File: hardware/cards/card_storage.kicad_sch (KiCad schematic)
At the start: 21 parts, among them J1 Conn_02x20_Odd_Even, J2 Conn_02x25_Odd_Even, U1 74HCT04, U10 74HCT573, U2 74HCT08, U3 74HCT08, U4 74HCT32, U5 74HCT125, U6 74HCT138, U7 74HCT138, U8 74HCT245, U9 74HCT573

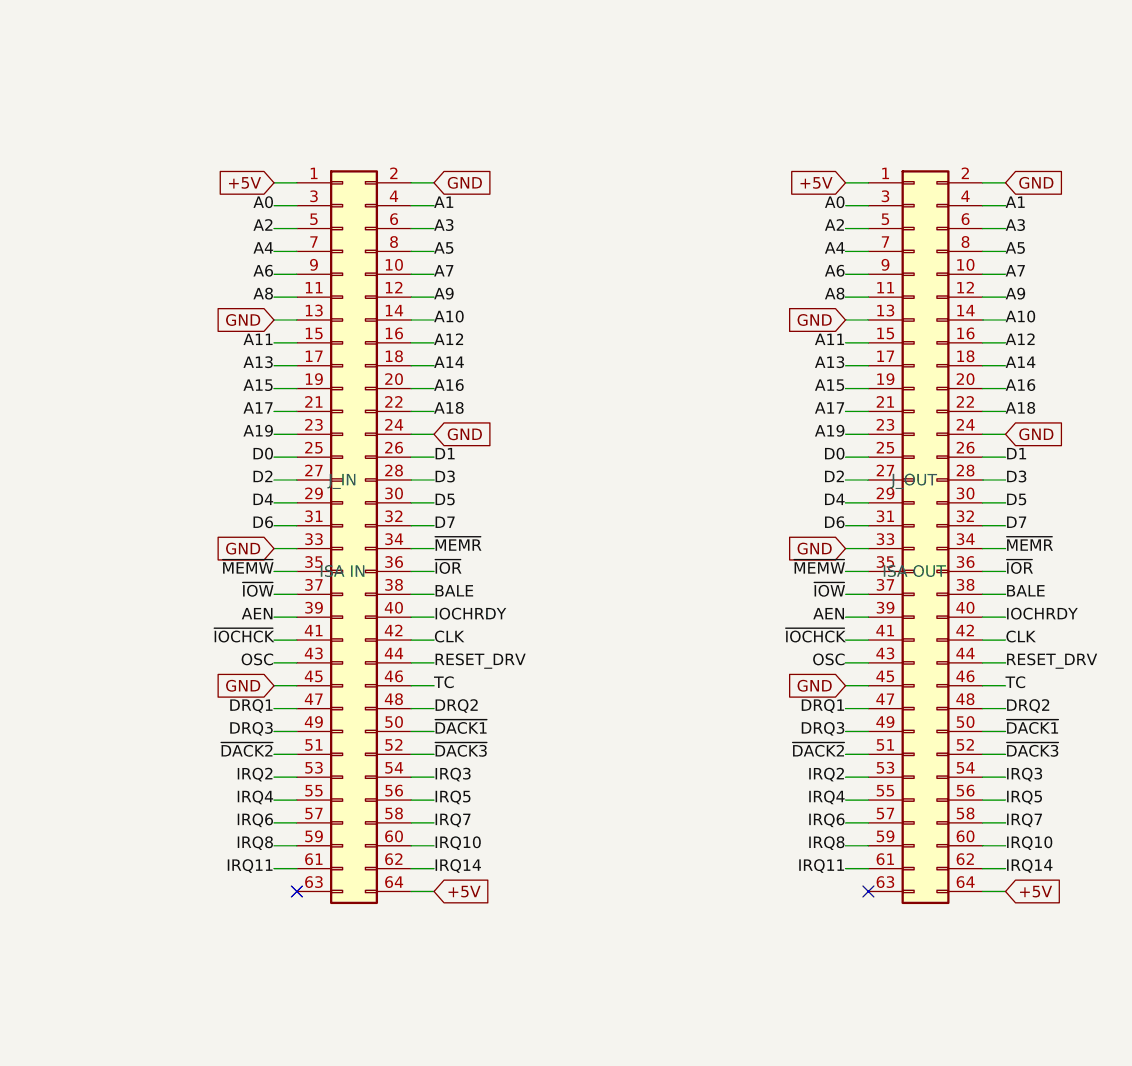
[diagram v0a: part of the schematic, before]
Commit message: Re-base ISA connector on standard 8-bit ISA pinout (60-pin, PicoGUS-style)
isa_conn now uses the standard 8-bit ISA edge pinout on a 60-pin 2.54mm header
(Conn_02x30_Odd_Even), matching the PicoGUS Bus_ISA_8bit layout so the sidecar and
dev cards are pin-compatible with real ISA cards (and 60-pin ribbon is easy to
source). The unused ISA analog rails are reclaimed: pin7 -5V->~{IOCHCK}, pin11
-12V->GND (extra return), pin15 +12V->IRQ8; pin13 reserved/0WS# left NC. Drops the
non-standard IRQ10/11/14 (16-bit-extension signals on a real AT); DACK0/REFRESH#
now on its standard pin (undriven, for card compatibility). Change is confined to
isa_conn.py; sidecar + all card_* sheets inherit it. Verified pin map and
connectivity (IOCHCK->Bus MCU, IRQ8->collector+RTC); zero structural ERC on
motherboard and all five cards.

Co-Authored-By: Claude Opus 4.8 (1M context) <noreply@anthropic.com>
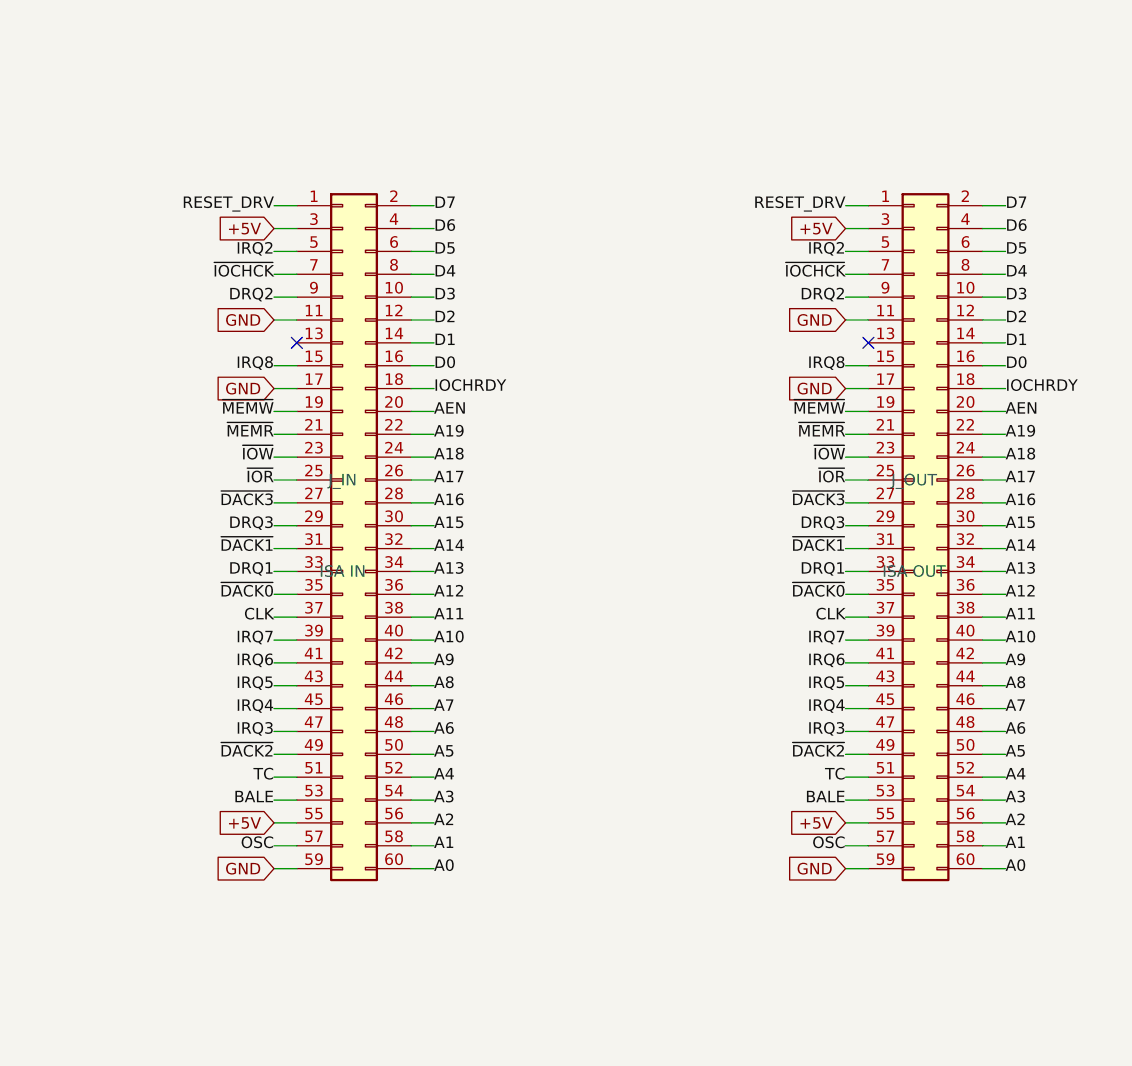
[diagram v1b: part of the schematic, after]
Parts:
- removed J_IN: ISA IN, symbol Connector_Generic:Conn_02x32_Odd_Even
- removed J_OUT: ISA OUT, symbol Connector_Generic:Conn_02x32_Odd_Even
- added J_IN: ISA IN, symbol Connector_Generic:Conn_02x30_Odd_Even
- added J_OUT: ISA OUT, symbol Connector_Generic:Conn_02x30_Odd_Even
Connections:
- net +5V: now also J_IN.3 (Pin_3), J_IN.55 (Pin_55), J_OUT.3 (Pin_3), J_OUT.55 (Pin_55)
- net A0: now also J_IN.60 (Pin_60), J_OUT.60 (Pin_60)
- net A1: now also J_IN.58 (Pin_58), J_OUT.58 (Pin_58)
- net A10: now also J_IN.40 (Pin_40), J_OUT.40 (Pin_40)
- net A11: now also J_IN.38 (Pin_38), J_OUT.38 (Pin_38)
- net A12: now also J_IN.36 (Pin_36), J_OUT.36 (Pin_36)
- net A13: now also J_IN.34 (Pin_34), J_OUT.34 (Pin_34)
- net A14: now also J_IN.32 (Pin_32), J_OUT.32 (Pin_32)
- net A15: now also J_IN.30 (Pin_30), J_OUT.30 (Pin_30)
- net A16: now also J_IN.28 (Pin_28), J_OUT.28 (Pin_28)
- net A17: now also J_IN.26 (Pin_26), J_OUT.26 (Pin_26)
- net A18: now also J_IN.24 (Pin_24), J_OUT.24 (Pin_24)
- net A19: now also J_IN.22 (Pin_22), J_OUT.22 (Pin_22)
- net A2: now also J_IN.56 (Pin_56), J_OUT.56 (Pin_56)
- net A3: now also J_IN.54 (Pin_54), J_OUT.54 (Pin_54)
- net A4: now also J_IN.52 (Pin_52), J_OUT.52 (Pin_52)
- net A5: now also J_IN.50 (Pin_50), J_OUT.50 (Pin_50)
- net A6: now also J_IN.48 (Pin_48), J_OUT.48 (Pin_48)
- net A7: now also J_IN.46 (Pin_46), J_OUT.46 (Pin_46)
- net A8: now also J_IN.44 (Pin_44), J_OUT.44 (Pin_44)
- net A9: now also J_IN.42 (Pin_42), J_OUT.42 (Pin_42)
- net AEN: now also J_IN.20 (Pin_20), J_OUT.20 (Pin_20)
- net BALE: now also J_IN.53 (Pin_53), J_OUT.53 (Pin_53)
- net CLK: now also J_IN.37 (Pin_37), J_OUT.37 (Pin_37)
- net D0: now also J_IN.16 (Pin_16), J_OUT.16 (Pin_16)
- net D1: now also J_IN.14 (Pin_14), J_OUT.14 (Pin_14)
- net D2: now also J_IN.12 (Pin_12), J_OUT.12 (Pin_12)
- net D3: now also J_IN.10 (Pin_10), J_OUT.10 (Pin_10)
- net D4: now also J_IN.8 (Pin_8), J_OUT.8 (Pin_8)
- net D5: now also J_IN.6 (Pin_6), J_OUT.6 (Pin_6)
- net D6: now also J_IN.4 (Pin_4), J_OUT.4 (Pin_4)
- net D7: now also J_IN.2 (Pin_2), J_OUT.2 (Pin_2)
- net DRQ1: now also J_IN.33 (Pin_33), J_OUT.33 (Pin_33)
- net DRQ2: now also J_IN.9 (Pin_9), J_OUT.9 (Pin_9)
- net DRQ3: now also J_IN.29 (Pin_29), J_OUT.29 (Pin_29)
- net GND: now also J_IN.11 (Pin_11), J_IN.17 (Pin_17), J_IN.59 (Pin_59), J_OUT.11 (Pin_11), J_OUT.17 (Pin_17), J_OUT.59 (Pin_59)
- net IOCHRDY: now also J_IN.18 (Pin_18), J_OUT.18 (Pin_18)
- net IRQ2: now also J_IN.5 (Pin_5), J_OUT.5 (Pin_5)
- net IRQ3: now also J_IN.47 (Pin_47), J_OUT.47 (Pin_47)
- net IRQ4: now also J_IN.45 (Pin_45), J_OUT.45 (Pin_45)
- net IRQ5: now also J_IN.43 (Pin_43), J_OUT.43 (Pin_43)
- net IRQ6: now also J_IN.41 (Pin_41), J_OUT.41 (Pin_41)
- net IRQ7: now also J_IN.39 (Pin_39), J_OUT.39 (Pin_39)
- net IRQ8: now also J_IN.15 (Pin_15), J_OUT.15 (Pin_15)
- net OSC: now also J_IN.57 (Pin_57), J_OUT.57 (Pin_57)
- net RESET_DRV: now also J_IN.1 (Pin_1), J_OUT.1 (Pin_1)
- net TC: now also J_IN.51 (Pin_51), J_OUT.51 (Pin_51)
- net ~{DACK1}: now also J_IN.31 (Pin_31), J_OUT.31 (Pin_31)
- net ~{DACK2}: now also J_IN.49 (Pin_49), J_OUT.49 (Pin_49)
- net ~{DACK3}: now also J_IN.27 (Pin_27), J_OUT.27 (Pin_27)
- net ~{IOCHCK}: now also J_IN.7 (Pin_7), J_OUT.7 (Pin_7)
- net ~{IOR}: now also J_IN.25 (Pin_25), J_OUT.25 (Pin_25)
- net ~{IOW}: now also J_IN.23 (Pin_23), J_OUT.23 (Pin_23)
- net ~{MEMR}: now also J_IN.21 (Pin_21), J_OUT.21 (Pin_21)
- net ~{MEMW}: now also J_IN.19 (Pin_19), J_OUT.19 (Pin_19)
- new net ~{DACK0}: J_IN.35 (Pin_35), J_OUT.35 (Pin_35)

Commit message: Drive ISA REFRESH# from the Bus MCU for DRAM-based cards
Pin 35 (DACK0/REFRESH#) net renamed ~{DACK0} -> ~{REFRESH} in isa_conn and is now
an active Bus MCU output (GPIO47, reclaimed from the redundant raw-~WR sense -- the
MCU tracks writes via the gated MEMW/IOW). Driven from the internal ~15us refresh
timer (same source as the 0x61-bit-4 toggle); a refresh cycle reuses the bus-master
engine to walk the row address on A0-A7 + pulse MEMR#, so DRAM ISA cards see a
standard refresh. ~{REFRESH} added to the Bus MCU interface. Verified it ties
sidecar<->Bus MCU and passes through J_IN<->J_OUT on every dev card; zero
structural ERC on motherboard and all five cards.

Co-Authored-By: Claude Opus 4.8 (1M context) <noreply@anthropic.com>
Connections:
- net ~{DACK0} renamed ~{REFRESH}
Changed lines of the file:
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@@
 		)
 	)
-	(label "~{DACK0}"
+	(label "~{REFRESH}"
 		(at 436.88 160.02 180)
 		(effects
@@
 		)
 	)
-	(label "~{DACK0}"
+	(label "~{REFRESH}"
 		(at 500.38 160.02 180)
 		(effects
@@
 		(instances
 			(project "card_storage"
-				(path "/ed5bbf70-1969-4673-8544-46a05cfa253c"
+				(path "/8a872234-6dda-4e68-94cb-1b220b28d7f7"
 					(reference "J_IN")
 					(unit 1)
@@
 		(instances
 			(project "card_storage"
-				(path "/ed5bbf70-1969-4673-8544-46a05cfa253c"
+				(path "/8a872234-6dda-4e68-94cb-1b220b28d7f7"
 					(reference "J_OUT")
 					(unit 1)
@@
 		(instances
 			(project "card_storage"
-				(path "/ed5bbf70-1969-4673-8544-46a05cfa253c"
+				(path "/8a872234-6dda-4e68-94cb-1b220b28d7f7"
 					(reference "U1")
 					(unit 1)
@@
 		(instances
 			(project "card_storage"
-				(path "/ed5bbf70-1969-4673-8544-46a05cfa253c"
+				(path "/8a872234-6dda-4e68-94cb-1b220b28d7f7"
 					(reference "U2")
 					(unit 1)
@@
 		(instances
 			(project "card_storage"
-				(path "/ed5bbf70-1969-4673-8544-46a05cfa253c"
+				(path "/8a872234-6dda-4e68-94cb-1b220b28d7f7"
 					(reference "U3")
 					(unit 1)
@@
 		(instances
 			(project "card_storage"
-				(path "/ed5bbf70-1969-4673-8544-46a05cfa253c"
+				(path "/8a872234-6dda-4e68-94cb-1b220b28d7f7"
 					(reference "U4")
 					(unit 1)
@@
 		(instances
 			(project "card_storage"
-				(path "/ed5bbf70-1969-4673-8544-46a05cfa253c"
+				(path "/8a872234-6dda-4e68-94cb-1b220b28d7f7"
 					(reference "U5")
 					(unit 1)
@@
 		(instances
 			(project "card_storage"
-				(path "/ed5bbf70-1969-4673-8544-46a05cfa253c"
+				(path "/8a872234-6dda-4e68-94cb-1b220b28d7f7"
 					(reference "U6")
 					(unit 1)
@@
 		(instances
 			(project "card_storage"
-				(path "/ed5bbf70-1969-4673-8544-46a05cfa253c"
+				(path "/8a872234-6dda-4e68-94cb-1b220b28d7f7"
 					(reference "U7")
 					(unit 1)
@@
 		(instances
 			(project "card_storage"
-				(path "/ed5bbf70-1969-4673-8544-46a05cfa253c"
+				(path "/8a872234-6dda-4e68-94cb-1b220b28d7f7"
 					(reference "U8")
 					(unit 1)
@@
 		(instances
 			(project "card_storage"
-				(path "/ed5bbf70-1969-4673-8544-46a05cfa253c"
+				(path "/8a872234-6dda-4e68-94cb-1b220b28d7f7"
 					(reference "U9")
 					(unit 1)
@@
 		(instances
 			(project "card_storage"
-				(path "/ed5bbf70-1969-4673-8544-46a05cfa253c"
+				(path "/8a872234-6dda-4e68-94cb-1b220b28d7f7"
 					(reference "U10")
 					(unit 1)
@@
 		(instances
 			(project "card_storage"
-				(path "/ed5bbf70-1969-4673-8544-46a05cfa253c"
+				(path "/8a872234-6dda-4e68-94cb-1b220b28d7f7"
 					(reference "J1")
 					(unit 1)
@@
 		(instances
 			(project "card_storage"
-				(path "/ed5bbf70-1969-4673-8544-46a05cfa253c"
+				(path "/8a872234-6dda-4e68-94cb-1b220b28d7f7"
 					(reference "J2")
 					(unit 1)
@@
 		(instances
 			(project "card_storage"
-				(path "/ed5bbf70-1969-4673-8544-46a05cfa253c"
+				(path "/8a872234-6dda-4e68-94cb-1b220b28d7f7"
 					(reference "R1")
 					(unit 1)
@@
 		(instances
 			(project "card_storage"
-				(path "/ed5bbf70-1969-4673-8544-46a05cfa253c"
+				(path "/8a872234-6dda-4e68-94cb-1b220b28d7f7"
 					(reference "R2")
 					(unit 1)
@@
 		(instances
 			(project "card_storage"
-				(path "/ed5bbf70-1969-4673-8544-46a05cfa253c"
+				(path "/8a872234-6dda-4e68-94cb-1b220b28d7f7"
 					(reference "R3")
 					(unit 1)
@@
 		(instances
 			(project "card_storage"
-				(path "/ed5bbf70-1969-4673-8544-46a05cfa253c"
+				(path "/8a872234-6dda-4e68-94cb-1b220b28d7f7"
 					(reference "C1")
 					(unit 1)
@@
 		(instances
 			(project "card_storage"
-				(path "/ed5bbf70-1969-4673-8544-46a05cfa253c"
+				(path "/8a872234-6dda-4e68-94cb-1b220b28d7f7"
 					(reference "C2")
 					(unit 1)
@@
 		(instances
 			(project "card_storage"
-				(path "/ed5bbf70-1969-4673-8544-46a05cfa253c"
+				(path "/8a872234-6dda-4e68-94cb-1b220b28d7f7"
 					(reference "C3")
 					(unit 1)
@@
 		(instances
 			(project "card_storage"
-				(path "/ed5bbf70-1969-4673-8544-46a05cfa253c"
+				(path "/8a872234-6dda-4e68-94cb-1b220b28d7f7"
 					(reference "C4")
 					(unit 1)

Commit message: Fix all critical+high design-review findings (C1-C5, H1-H8)
Full review in hardware/notes/design-review-2026-07-03.md (with per-item
fix logs). Highlights:
- SRAM strobed by gated MEMR/MEMW (was raw ~RD/~WR: I/O cycles corrupted
  SRAM and the boot shadow-load could never write it)
- Reset chain implemented: NAND combine of ~PWRGOOD + ~CPURESET drives
  V20 RESET and an always-driven RESET_DRV (dropped from the Bus MCU)
- Contention-free bus handoff: '573 OE=HLDA vs counter '244 stage
  ~OE=~HLDA; strobe gates wired + tri-stated ('125, ~OE=HLDA); Bus MCU
  address group fixed to sense; AEN/TC fixed drive; BALE input-only
- '573 LE driven by BALE (was a dangling BALE_L label)
- Data '245 DIR=DT/~R, ~OE=DEN so INTA vectors reach the CPU
- Idle pulls: strobes/DEN high, AEN/IRQ2-9/DRQ low, IOCHRDY/IOCHCK/
  DACK2-3 high
- CH224K CFG1 left open (grounding it selects 9-20V, not 5V)
- XT-IDE INTRQ pull-down (pull-up parked IRQ5 asserted)
- LPT status bit7 = ~Busy via spare inverter (SPP semantics)
- Audio summer TL072 -> MCP6002 (RRIO; TL072 out of spec at +5V single
  supply)
- card_isatest: DUT P-FET gate to V5RAW + NPN driver (default off, can
  fully turn off); /3 divider TC->~PE reload actually wired

Overturned picks corrected in notes/questions-*.md. All sheets + cards
rebuilt; structural ERC = 0; fixes netlist-verified.

Co-Authored-By: Claude Fable 5 <noreply@anthropic.com>
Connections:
- net +5V: no longer R2.1
- net GND: now also R2.2
- net IDE_IRQ: now also R2.1; no longer R2.2
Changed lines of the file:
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@@
 		)
 	)
-	(global_label "+5V"
-		(shape input)
+	(label "IDE_IRQ"
 		(at 243.84 19.05 90)
 		(effects
@@
 		)
 	)
-	(label "IDE_IRQ"
+	(global_label "GND"
+		(shape input)
 		(at 243.84 31.75 270)
 		(effects
@@
 		(instances
 			(project "card_storage"
-				(path "/e735f188-f9b6-453d-9c9a-0564fbf31343"
+				(path "/6e45eab2-d93d-420b-a499-bad246ff05e1"
 					(reference "J_IN")
 					(unit 1)
@@
 		(instances
 			(project "card_storage"
-				(path "/e735f188-f9b6-453d-9c9a-0564fbf31343"
+				(path "/6e45eab2-d93d-420b-a499-bad246ff05e1"
 					(reference "J_OUT")
 					(unit 1)
@@
 		(instances
 			(project "card_storage"
-				(path "/e735f188-f9b6-453d-9c9a-0564fbf31343"
+				(path "/6e45eab2-d93d-420b-a499-bad246ff05e1"
 					(reference "U1")
 					(unit 1)
@@
 		(instances
 			(project "card_storage"
-				(path "/e735f188-f9b6-453d-9c9a-0564fbf31343"
+				(path "/6e45eab2-d93d-420b-a499-bad246ff05e1"
 					(reference "U2")
 					(unit 1)
@@
 		(instances
 			(project "card_storage"
-				(path "/e735f188-f9b6-453d-9c9a-0564fbf31343"
+				(path "/6e45eab2-d93d-420b-a499-bad246ff05e1"
 					(reference "U3")
 					(unit 1)
@@
 		(instances
 			(project "card_storage"
-				(path "/e735f188-f9b6-453d-9c9a-0564fbf31343"
+				(path "/6e45eab2-d93d-420b-a499-bad246ff05e1"
 					(reference "U4")
 					(unit 1)
@@
 		(instances
 			(project "card_storage"
-				(path "/e735f188-f9b6-453d-9c9a-0564fbf31343"
+				(path "/6e45eab2-d93d-420b-a499-bad246ff05e1"
 					(reference "U5")
 					(unit 1)
@@
 		(instances
 			(project "card_storage"
-				(path "/e735f188-f9b6-453d-9c9a-0564fbf31343"
+				(path "/6e45eab2-d93d-420b-a499-bad246ff05e1"
 					(reference "U6")
 					(unit 1)
@@
 		(instances
 			(project "card_storage"
-				(path "/e735f188-f9b6-453d-9c9a-0564fbf31343"
+				(path "/6e45eab2-d93d-420b-a499-bad246ff05e1"
 					(reference "U7")
 					(unit 1)
@@
 		(instances
 			(project "card_storage"
-				(path "/e735f188-f9b6-453d-9c9a-0564fbf31343"
+				(path "/6e45eab2-d93d-420b-a499-bad246ff05e1"
 					(reference "U8")
 					(unit 1)
@@
 		(instances
 			(project "card_storage"
-				(path "/e735f188-f9b6-453d-9c9a-0564fbf31343"
+				(path "/6e45eab2-d93d-420b-a499-bad246ff05e1"
 					(reference "U9")
 					(unit 1)
@@
 		(instances
 			(project "card_storage"
-				(path "/e735f188-f9b6-453d-9c9a-0564fbf31343"
+				(path "/6e45eab2-d93d-420b-a499-bad246ff05e1"
 					(reference "U10")
 					(unit 1)
@@
 		(instances
 			(project "card_storage"
-				(path "/e735f188-f9b6-453d-9c9a-0564fbf31343"
+				(path "/6e45eab2-d93d-420b-a499-bad246ff05e1"
 					(reference "J1")
 					(unit 1)
@@
 		(instances
 			(project "card_storage"
-				(path "/e735f188-f9b6-453d-9c9a-0564fbf31343"
+				(path "/6e45eab2-d93d-420b-a499-bad246ff05e1"
 					(reference "J2")
 					(unit 1)
@@
 		(instances
 			(project "card_storage"
-				(path "/e735f188-f9b6-453d-9c9a-0564fbf31343"
+				(path "/6e45eab2-d93d-420b-a499-bad246ff05e1"
 					(reference "R1")
 					(unit 1)
@@
 		(instances
 			(project "card_storage"
-				(path "/e735f188-f9b6-453d-9c9a-0564fbf31343"
+				(path "/6e45eab2-d93d-420b-a499-bad246ff05e1"
 					(reference "R2")
 					(unit 1)
@@
 		(instances
 			(project "card_storage"
-				(path "/e735f188-f9b6-453d-9c9a-0564fbf31343"
+				(path "/6e45eab2-d93d-420b-a499-bad246ff05e1"
 					(reference "R3")
 					(unit 1)
@@
 		(instances
 			(project "card_storage"
-				(path "/e735f188-f9b6-453d-9c9a-0564fbf31343"
+				(path "/6e45eab2-d93d-420b-a499-bad246ff05e1"
 					(reference "C1")
 					(unit 1)
@@
 		(instances
 			(project "card_storage"
-				(path "/e735f188-f9b6-453d-9c9a-0564fbf31343"
+				(path "/6e45eab2-d93d-420b-a499-bad246ff05e1"
 					(reference "C2")
 					(unit 1)
@@
 		(instances
 			(project "card_storage"
-				(path "/e735f188-f9b6-453d-9c9a-0564fbf31343"
+				(path "/6e45eab2-d93d-420b-a499-bad246ff05e1"
 					(reference "C3")
 					(unit 1)
@@
 		(instances
 			(project "card_storage"
-				(path "/e735f188-f9b6-453d-9c9a-0564fbf31343"
+				(path "/6e45eab2-d93d-420b-a499-bad246ff05e1"
 					(reference "C4")
 					(unit 1)

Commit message: Fix all medium design-review findings (M1-M8)
- M1: Supervisor link moved to GPIO4/5 (real UART1 pair); POST -> GPIO6-15
- M2: CNT_RUN = LD0.LD1.LD2 gates every '163 CEP (load-cascade hazard)
- M3: ~WR / IO-M pruned to cpu_core-internal; DRQ2/3 pulled + noted;
  doc S5.2 "as built: 48/48" + S16 updated
- M4: true XT-IDE rev-2 map (A0<->A3 swap): data 0x300, latch 0x301,
  CS1 0x307/0x30F, drive DA0 = bus A3 - matches XTIDE UB "rev 2" type
- M5: COM4 -> bus IRQ2 line (IRQ9 via AT redirect); IRQ10/11/14/15 marked
  off-header; ~REFRESH added to mxbus ISA_CTRL; questions-sidecar superseded
- M6: card_isatest clock tree on unswitched V5RAW (spec S8)
- M7: card_isatest IRQ2-8/DRQ1-3 idle pull-downs (spec S4/S9)
- M8: com_port JP1 selects 16550 RX source (DB9 vs TTL console); 5V note

Rebuilt motherboard + cards; structural ERC = 0; netlist-verified.
Fix log in hardware/notes/design-review-2026-07-03.md (batch 3).

Co-Authored-By: Claude Fable 5 <noreply@anthropic.com>
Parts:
- added U11: 74HCT138, symbol mini-xt:74HCT138
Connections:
- net +5V: now also U11.16 (VCC), U11.6 (E2)
- net A0: now also U6.1 (A0); no longer J1.35 (Pin_35), J2.20 (Pin_20), U7.1 (A0)
- net A1: now also U7.1 (A0), U11.1 (A0); no longer U7.2 (A1)
- net A2: now also U7.2 (A1), U11.2 (A1); no longer U7.3 (A2)
- net A3: now also J1.35 (Pin_35), J2.20 (Pin_20), U7.3 (A2), U11.3 (A2); no longer U6.1 (A0)
- net GND: now also U11.5 (~{E1}), U11.8 (GND)
- net ~{DATA_SEL}: now also U11.15 (~{Y0}); no longer U7.15 (~{Y0})
- net ~{HB_SEL}: now also U7.15 (~{Y0}); no longer U6.13 (~{Y2})
- net ~{IDE_CS0}: now also U11.4 (~{E0}); no longer U7.4 (~{E0})
- net ~{IDE_CS1}: now also U3.6 (P6); no longer U6.14 (~{Y1})
- net ~{CS1_A}: now reaches U3.4 (P4)
- net ~{CS1_A}: now also U7.12 (~{Y3})
- net ~{CS1_B}: now reaches U3.5 (P5)
- net ~{CS1_B}: now also U7.7 (~{Y7})
- new net ~{ODD_SEL}: U6.14 (~{Y1}), U7.4 (~{E0})
- no-connect marks 42 -> 46
